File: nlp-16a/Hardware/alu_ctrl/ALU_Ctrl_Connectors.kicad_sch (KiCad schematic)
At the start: 85 parts, among them J1 Screw_Terminal_01x02, J10 Conn_02x08_Odd_Even, J2 Conn_02x20_Odd_Even, J3 Conn_02x10_Counter_Clockwise, J4 Conn_02x10_Counter_Clockwise, J5 Conn_02x10_Counter_Clockwise, J6 Conn_02x10_Counter_Clockwise, J7 Conn_02x10_Counter_Clockwise, J8 Conn_02x08_Odd_Even, J9 Conn_02x08_Odd_Even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

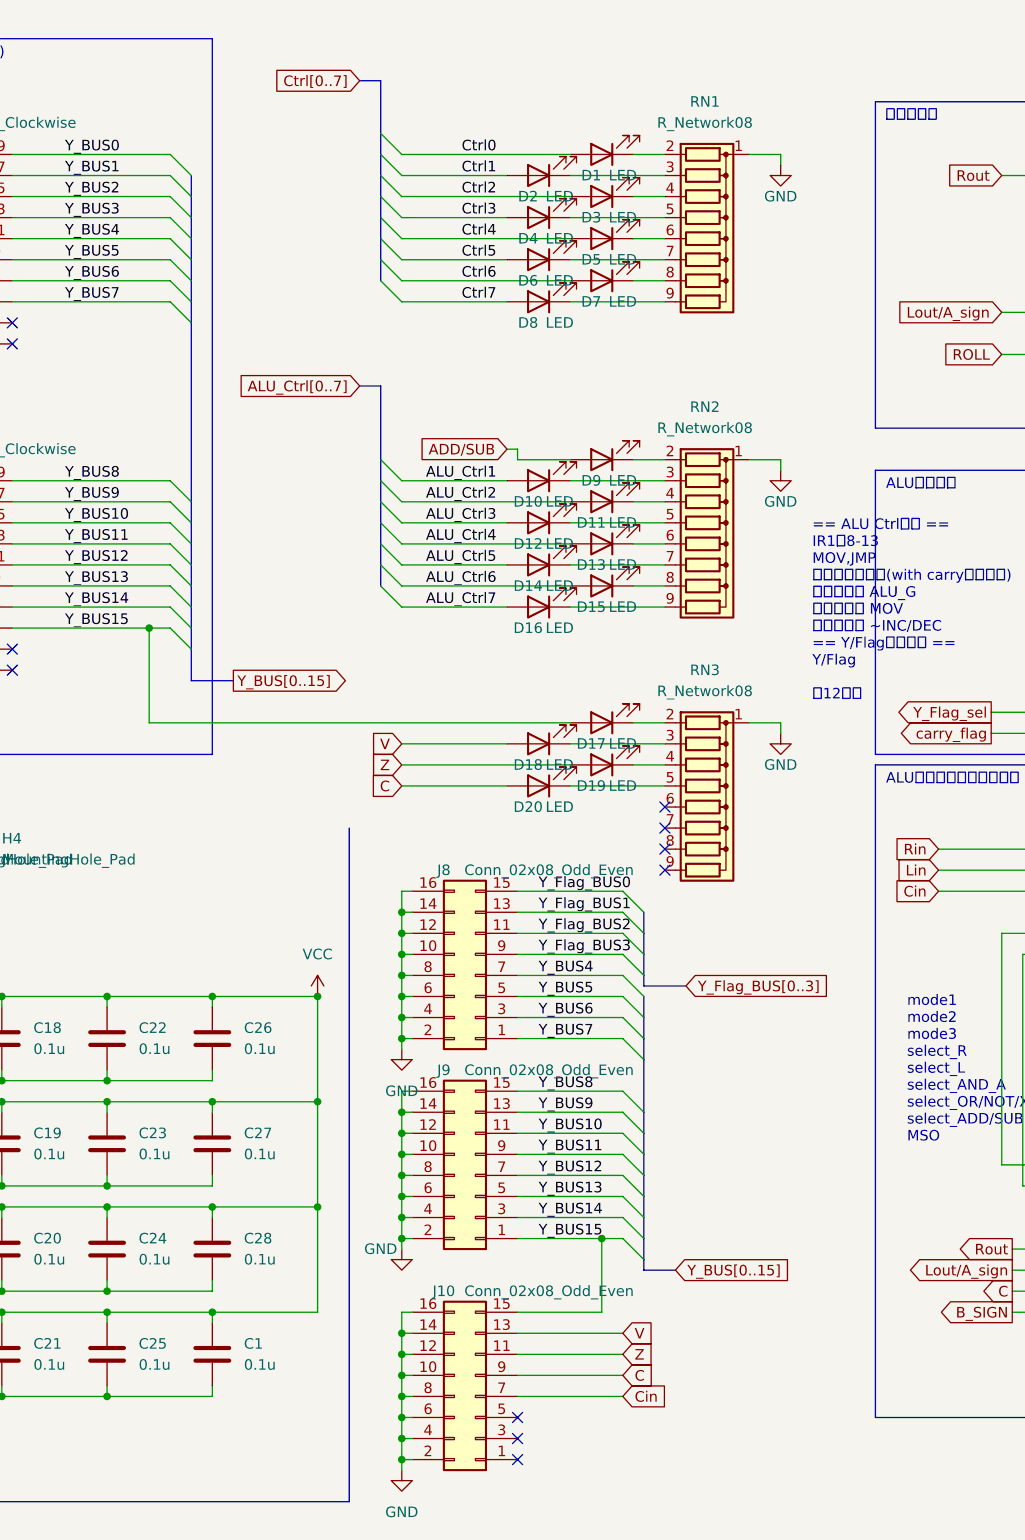
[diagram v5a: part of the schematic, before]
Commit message: 電源バスの引き直しとデバッグポートの配線完了
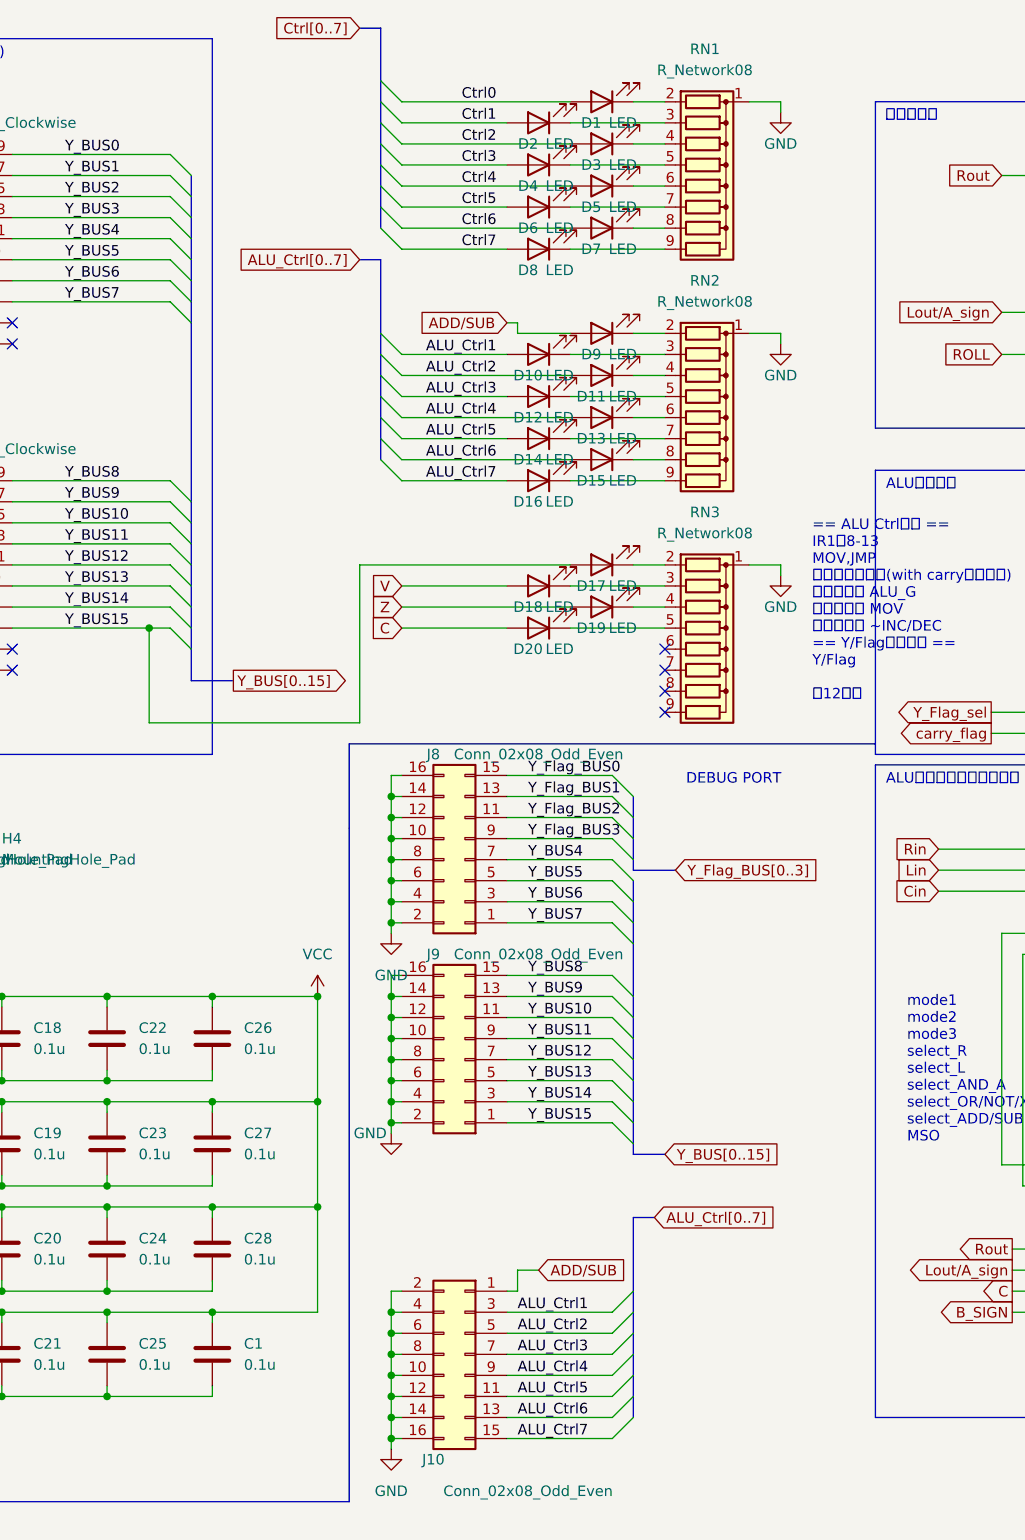
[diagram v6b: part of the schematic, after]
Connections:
- net ADD/SUB: now also J10.1 (Pin_1)
- net ALU_Ctrl1: now also J10.3 (Pin_3)
- net ALU_Ctrl2: now also J10.5 (Pin_5)
- net ALU_Ctrl3: now also J10.7 (Pin_7)
- net ALU_Ctrl4: now also J10.9 (Pin_9)
- net ALU_Ctrl5: now also J10.11 (Pin_11)
- net ALU_Ctrl6: now also J10.13 (Pin_13)
- net ALU_Ctrl7: now also J10.15 (Pin_15)
- net C: no longer J10.9 (Pin_9)
- net Cin: no longer J10.7 (Pin_7)
- net V: no longer J10.13 (Pin_13)
- net Y_BUS15: no longer J10.15 (Pin_15)
- net Z: no longer J10.11 (Pin_11)
- no-connect marks 34 -> 31
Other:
- note added: "DEBUG PORT"
- moved on the sheet: D1, D10, D11, D12, D13, D14, D15, D16, D17, D18, D19, D2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

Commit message: だいたい完成．残りは詳細チェックとビア打ち
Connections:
- net V: now also D19.2 (A); no longer D18.2 (A)
- net Z: now also D18.2 (A); no longer D19.2 (A)
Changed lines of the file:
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@@
+    (stroke (width 0) (type default) (color 0 0 0 0))
+  )
+  (wire (pts (xy 147.32 86.36) (xy 160.02 86.36))
     (stroke (width 0) (type default) (color 0 0 0 0))
   )
@@
     (stroke (width 0) (type default) (color 0 0 0 0))
   )
+  (wire (pts (xy 142.24 78.74) (xy 167.64 78.74))
+    (stroke (width 0) (type default) (color 0 0 0 0))
+  )
   (wire (pts (xy 261.62 111.76) (xy 261.62 113.03))
     (stroke (width 0) (type default) (color 0 0 0 0))
@@
     (stroke (width 0) (type default) (color 0 0 0 0))
   )
-  (wire (pts (xy 147.32 86.36) (xy 160.02 86.36))
-    (stroke (width 0) (type default) (color 0 0 0 0))
-  )
   (wire (pts (xy 73.66 168.91) (xy 86.36 168.91))
     (stroke (width 0) (type default) (color 0 0 0 0))
@@
     (stroke (width 0) (type default) (color 0 0 0 0))
   )
-  (wire (pts (xy 142.24 78.74) (xy 167.64 78.74))
-    (stroke (width 0) (type default) (color 0 0 0 0))
-  )
   (wire (pts (xy 243.84 50.8) (xy 243.84 53.34))
     (stroke (width 0) (type default) (color 0 0 0 0))
@@
     (stroke (width 0) (type default) (color 0 0 0 0))
   )
-  (wire (pts (xy 142.24 97.79) (xy 142.24 78.74))
+  (wire (pts (xy 142.24 78.74) (xy 142.24 97.79))
     (stroke (width 0) (type default) (color 0 0 0 0))
   )
@@
     )
   )
-  (global_label "V" (shape input) (at 147.32 81.28 180) (fields_autoplaced)
+  (global_label "V" (shape input) (at 147.32 83.82 180) (fields_autoplaced)
     (effects (font (size 1.27 1.27)) (justify right))
-    (property "Intersheet References" "${INTERSHEET_REFS}" (id 0) (at 143.8183 81.2006 0)
+    (property "Intersheet References" "${INTERSHEET_REFS}" (id 0) (at 143.8183 83.7406 0)
       (effects (font (size 1.27 1.27)) (justify right) hide)
     )
@@
     )
   )
-  (global_label "Z" (shape input) (at 147.32 83.82 180) (fields_autoplaced)
+  (global_label "Z" (shape input) (at 147.32 81.28 180) (fields_autoplaced)
     (effects (font (size 1.27 1.27)) (justify right))
-    (property "Intersheet References" "${INTERSHEET_REFS}" (id 0) (at 143.6974 83.7406 0)
+    (property "Intersheet References" "${INTERSHEET_REFS}" (id 0) (at 143.6974 81.2006 0)
       (effects (font (size 1.27 1.27)) (justify right) hide)
     )

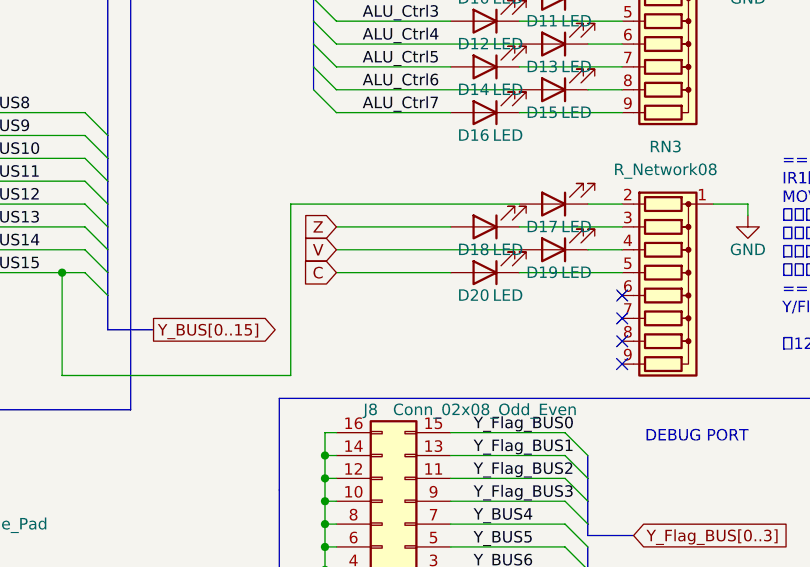
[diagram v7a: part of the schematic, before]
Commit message: 先ほどのオーバーフロー検出部の不具合を修正
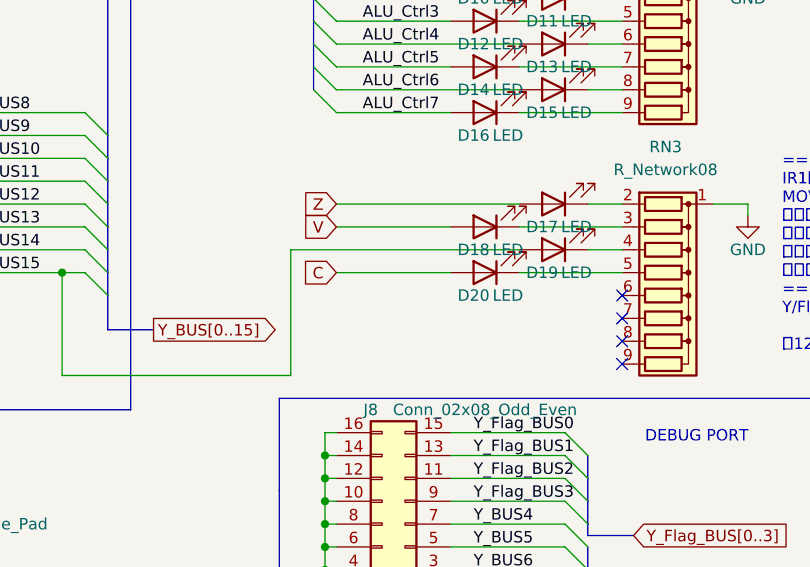
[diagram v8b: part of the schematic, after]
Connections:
- net V: now also D18.2 (A); no longer D19.2 (A)
- net Y_BUS15: now also D19.2 (A); no longer D17.2 (A)
- net Z: now also D17.2 (A); no longer D18.2 (A)
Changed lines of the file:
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@@
+    (stroke (width 0) (type default) (color 0 0 0 0))
+  )
+  (wire (pts (xy 142.24 83.82) (xy 167.64 83.82))
     (stroke (width 0) (type default) (color 0 0 0 0))
   )
@@
     (stroke (width 0) (type default) (color 0 0 0 0))
   )
-  (wire (pts (xy 147.32 83.82) (xy 167.64 83.82))
-    (stroke (width 0) (type default) (color 0 0 0 0))
-  )
   (bus (pts (xy 121.92 41.91) (xy 121.92 44.45))
     (stroke (width 0) (type default) (color 0 0 0 0))
@@
     (stroke (width 0) (type default) (color 0 0 0 0))
   )
+  (wire (pts (xy 142.24 83.82) (xy 142.24 97.79))
+    (stroke (width 0) (type default) (color 0 0 0 0))
+  )
   (wire (pts (xy 111.76 177.8) (xy 111.76 179.07))
     (stroke (width 0) (type default) (color 0 0 0 0))
@@
     (stroke (width 0) (type default) (color 0 0 0 0))
   )
-  (wire (pts (xy 142.24 78.74) (xy 167.64 78.74))
-    (stroke (width 0) (type default) (color 0 0 0 0))
-  )
   (wire (pts (xy 261.62 111.76) (xy 261.62 113.03))
     (stroke (width 0) (type default) (color 0 0 0 0))
@@
     (stroke (width 0) (type default) (color 0 0 0 0))
   )
+  (wire (pts (xy 147.32 78.74) (xy 167.64 78.74))
+    (stroke (width 0) (type default) (color 0 0 0 0))
+  )
   (wire (pts (xy 124.46 168.91) (xy 124.46 170.18))
     (stroke (width 0) (type default) (color 0 0 0 0))
@@
   )
   (wire (pts (xy 245.11 96.52) (xy 259.08 96.52))
-    (stroke (width 0) (type default) (color 0 0 0 0))
-  )
-  (wire (pts (xy 142.24 78.74) (xy 142.24 97.79))
     (stroke (width 0) (type default) (color 0 0 0 0))
   )
@@
     )
   )
-  (global_label "V" (shape input) (at 147.32 83.82 180) (fields_autoplaced)
+  (global_label "V" (shape input) (at 147.32 81.28 180) (fields_autoplaced)
     (effects (font (size 1.27 1.27)) (justify right))
-    (property "Intersheet References" "${INTERSHEET_REFS}" (id 0) (at 143.8183 83.7406 0)
+    (property "Intersheet References" "${INTERSHEET_REFS}" (id 0) (at 143.8183 81.2006 0)
       (effects (font (size 1.27 1.27)) (justify right) hide)
     )
@@
     )
   )
-  (global_label "Z" (shape input) (at 147.32 81.28 180) (fields_autoplaced)
+  (global_label "Z" (shape input) (at 147.32 78.74 180) (fields_autoplaced)
     (effects (font (size 1.27 1.27)) (justify right))
-    (property "Intersheet References" "${INTERSHEET_REFS}" (id 0) (at 143.6974 81.2006 0)
+    (property "Intersheet References" "${INTERSHEET_REFS}" (id 0) (at 143.6974 78.6606 0)
       (effects (font (size 1.27 1.27)) (justify right) hide)
     )
